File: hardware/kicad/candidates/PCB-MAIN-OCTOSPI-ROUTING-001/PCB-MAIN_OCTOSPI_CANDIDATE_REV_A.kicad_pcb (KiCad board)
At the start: 6 copper layers, 110 x 75 mm, 251 parts, among them J10 U.FL-R-SMT-1(60), J11 USB4105-GF-A-120, J12 MEM2052-00-195-00-A, J13 504050-0291, J6 2336582-1, J7 2336582-1, J8 U.FL-R-SMT-1(60), J9 U.FL-R-SMT-1(60), Q1 MMBT3904,215, Q2 MMBT3904,215, Q3 MMBT3904,215, Q4 Si1016X-T1-GE3, U1 STM32U585VIT6Q, U10 E22-900M22S, U11 MDBT50Q-P1MV2, U13 TS3A27518EPWR, U14 ESDALC6V1-5P6, U15 ESDALC6V1-5P6, U16 SN74AXC8T245PWR, U17 SN74LVC32APWR, U18 SN74AXC1T45DRLR, U19 TPD4E05U06DQAR, U2 W25Q512JVFIQ, U20 TPD4E05U06DQAR, U21 TPD4E05U06DQAR, U22 TPD4E05U06DQAR, U23 TPD4E05U06DQAR, U24 TPD4E05U06DQAR, U25 TPD2EUSB30DRTR, U26 TPD2EUSB30DRTR, U27 TPD4E05U06DQAR, U3 LIS2DW12TR, U4 STTS22HTR, U5 LT6000IDCB#TRMPBF, U6 SN74LVC1G07DBVR, U7 SN74AXC8T245PWR, U8 BG95-M3, U9 MAX-M10S-00B, X1 SiT1552AI-JE-DCC-32.768D

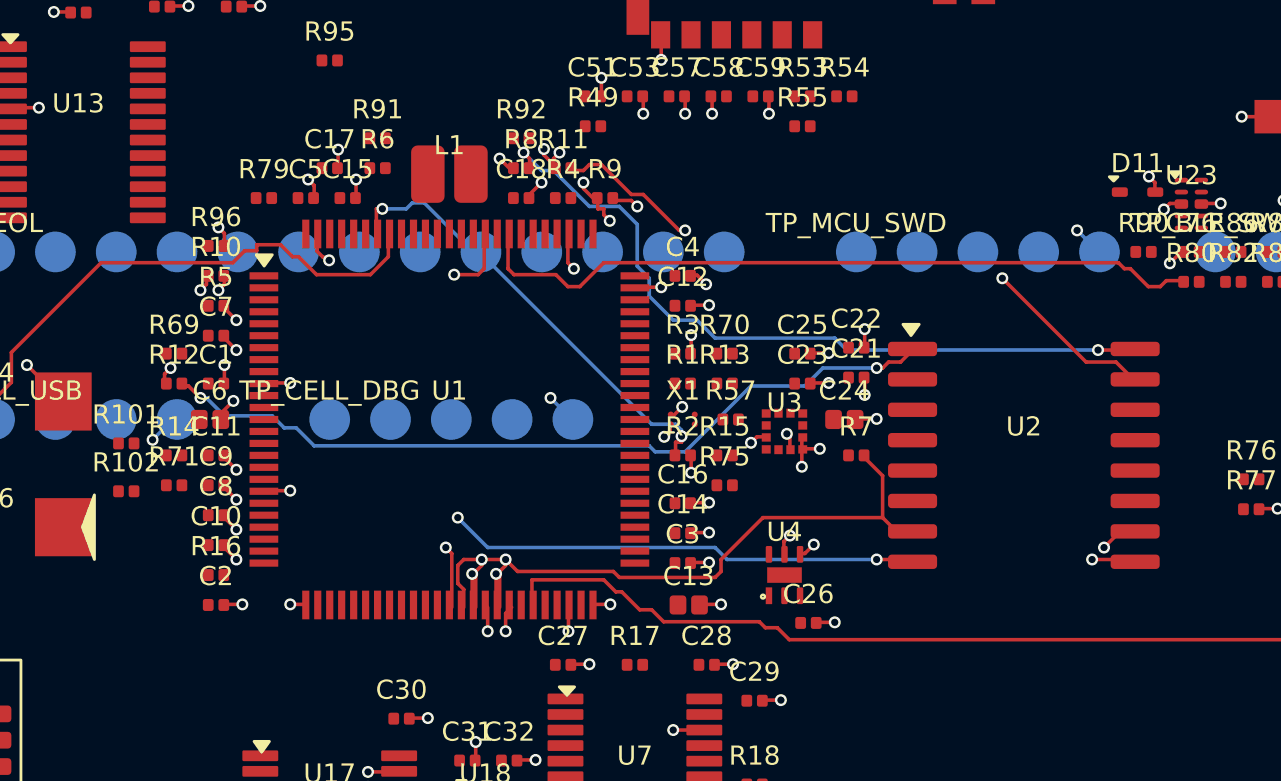
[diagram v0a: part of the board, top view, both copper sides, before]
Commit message: hardware: correct PCB-MAIN OctoSPI routing clearance
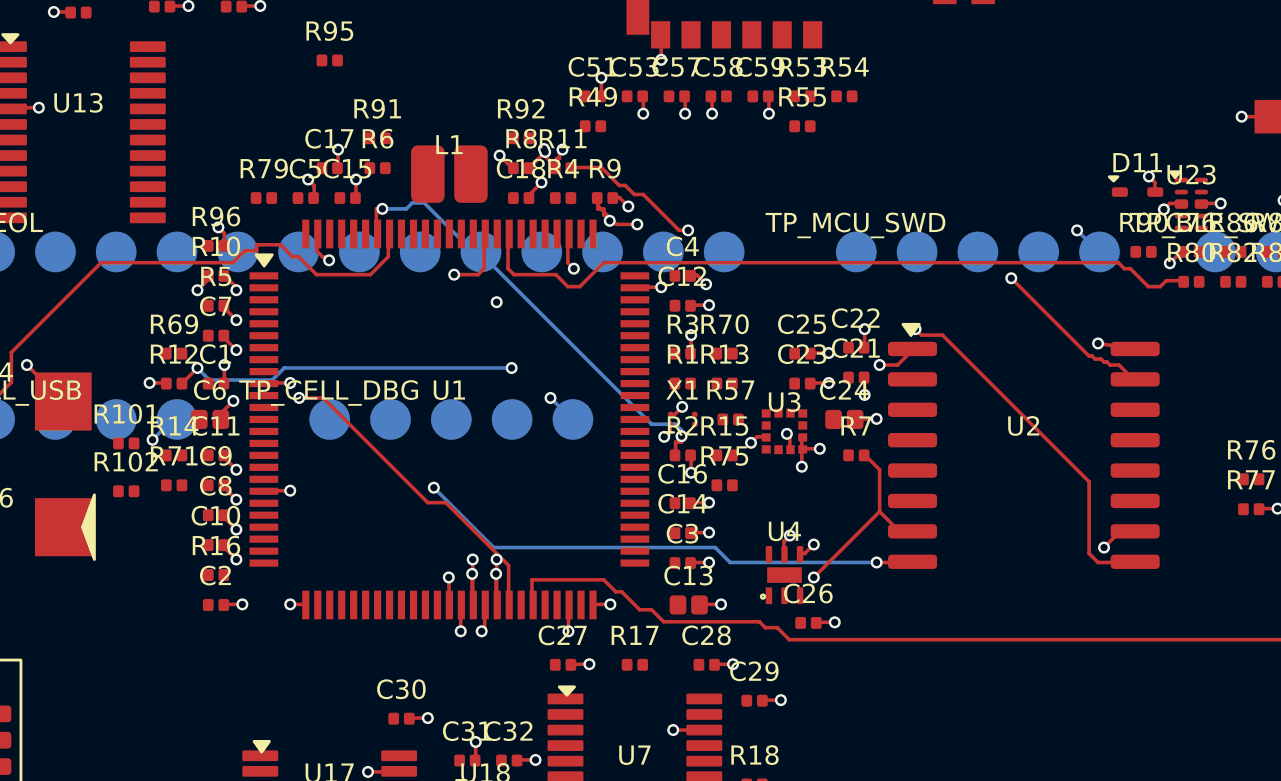
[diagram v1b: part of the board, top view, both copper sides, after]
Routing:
- net NOR_CLK_U2: track 31.2 -> 28.9 mm
- net NOR_IO3_U2: track 33.4 -> 31.5 mm, vias 2 -> 3
- net NOR_IO0_U1: track 40.6 -> 42.1 mm
- net NOR_IO2_U2: track 31.2 -> 32.1 mm
- net NOR_IO3_U1: track 21.1 -> 20.5 mm
- net NOR_NCS_U2: track 25.6 -> 25.1 mm, vias 0 -> 2
- net NOR_IO2_U1: track 41.7 -> 41.9 mm, vias 4 -> 5
